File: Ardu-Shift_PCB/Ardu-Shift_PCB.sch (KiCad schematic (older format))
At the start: 18 parts, among them U1 OLED(SPI), U2 Arduino_Pro_Micro

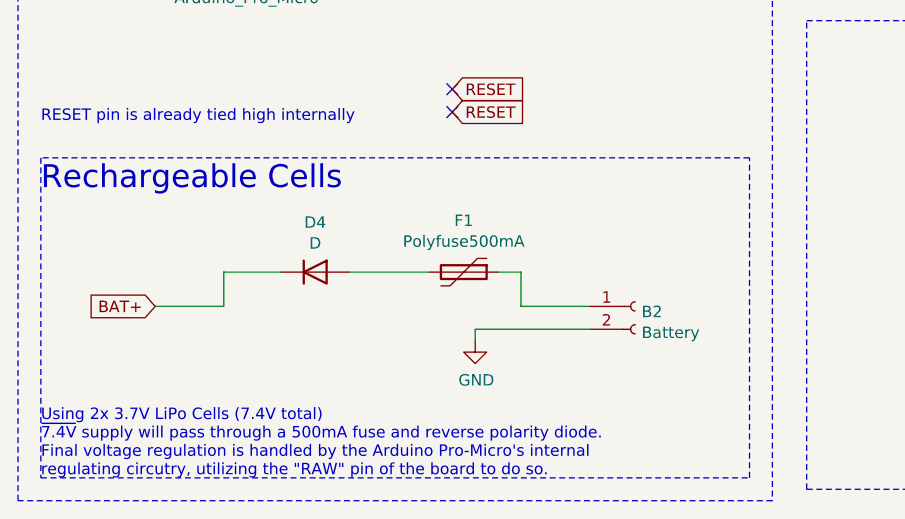
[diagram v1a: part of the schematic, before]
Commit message: added a power switch to ground for on/off functionality, added footprint for smaller speaker and updated all files.PDFs
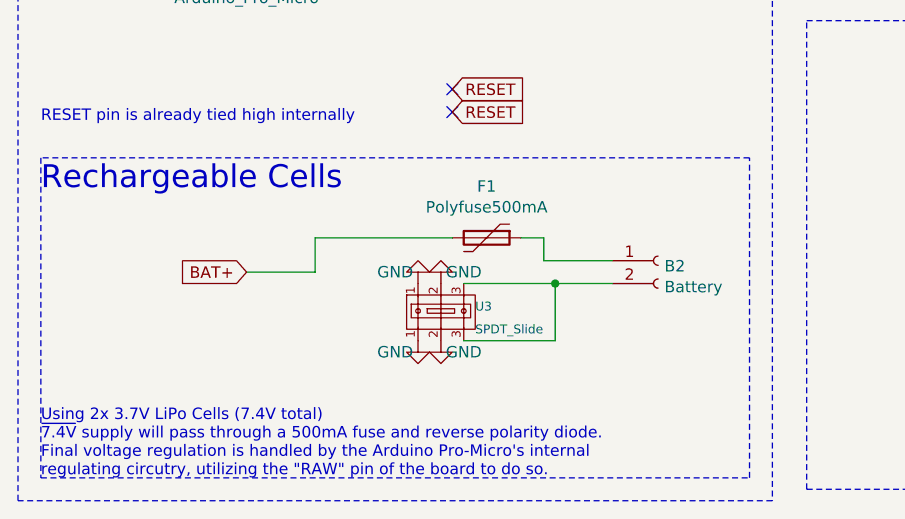
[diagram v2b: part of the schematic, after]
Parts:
- removed D4: D, Diode_THT:D_A-405_P10.16mm_Horizontal, symbol Device:D
- added U3: SPDT_Slide, Button_Switch_THT:SPDT_Slide, symbol Connector_Generic:SPDT_Slide
- LS1: footprint Resistor_THT:R_Axial_DIN0411_L9.9mm_D3.6mm_P15.24mm_Horizontal -> Buzzer_Beeper:Buzzer_12x9.5RM7.6
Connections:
- net BAT+: now also F1.2
- net GND: now also U3.1, U3.2; no longer B2.2 (Pin_2)
- new net: B2.2 (Pin_2), U3.3
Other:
- moved on the sheet: B2, F1
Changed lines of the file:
@@
 F 0 "LS1" V 3209 720 50  0000 R CNN
 F 1 "Speaker" V 3118 720 50  0000 R CNN
-F 2 "Resistor_THT:R_Axial_DIN0411_L9.9mm_D3.6mm_P15.24mm_Horizontal" H 3200 800 50  0001 C CNN
+F 2 "Buzzer_Beeper:Buzzer_12x9.5RM7.6" H 3200 800 50  0001 C CNN
 F 3 "~" H 3190 950 50  0001 C CNN
 	1    3200 1000
@@
 Text Notes 4200 800  0    100  ~ 0
 User Inputs\n
-Text GLabel 1250 6750 0    50   Input ~ 0
+Text GLabel 1650 6600 0    50   Input ~ 0
 BAT+
 Wire Notes Line
@@
 L Connector:Conn_01x02_Female B2
 U 1 1 603C890C
-P 3350 6750
-F 0 "B2" H 3378 6726 50  0000 L CNN
-F 1 "Battery" H 3378 6635 50  0000 L CNN
-F 2 "Connector_PinHeader_2.54mm:PinHeader_1x02_P2.54mm_Vertical" H 3350 6750 50  0001 C CNN
-F 3 "~" H 3350 6750 50  0001 C CNN
-	1    3350 6750
+P 3450 6550
+F 0 "B2" H 3478 6526 50  0000 L CNN
+F 1 "Battery" H 3478 6435 50  0000 L CNN
+F 2 "Connector_PinHeader_2.54mm:PinHeader_1x02_P2.54mm_Vertical" H 3450 6550 50  0001 C CNN
+F 3 "~" H 3450 6550 50  0001 C CNN
+	1    3450 6550
 	1    0    0    -1
 $EndComp
@@
 Wire Notes Line
 	3950 3650 3950 7600
-Text Notes 750  7500 0    50   ~ 0
-Using 2x 3.7V LiPo Cells (7.4V total)\n~7.4V supply will pass through a 500mA fuse and reverse polarity diode.\nFinal voltage regulation is handled by the Arduino Pro-Micro's internal \nregulating circutry, utilizing the "RAW" pin of the board to do so.
 Text Notes 800  3200 0    50   ~ 0
 Will be using THT for LEDs, Resistors, and Speaker \nTODO** determine resistor values for the LEDs michael has on hand\n
@@
 L Device:Polyfuse F1
 U 1 1 6044FB48
-P 2600 6600
-F 0 "F1" V 2375 6600 50  0000 C CNN
-F 1 "Polyfuse500mA" V 2466 6600 50  0000 C CNN
-F 2 "Resistor_THT:R_Axial_DIN0207_L6.3mm_D2.5mm_P7.62mm_Horizontal" H 2650 6400 50  0001 L CNN
-F 3 "~" H 2600 6600 50  0001 C CNN
-	1    2600 6600
-	0    1    1    0
-$EndComp
-Wire Wire Line
-	2750 6600 2850 6600
-Wire Wire Line
-	2850 6600 2850 6750
-Wire Wire Line
-	2850 6750 3150 6750
-$Comp
-L Device:D D4
-U 1 1 604552AC
-P 1950 6600
-F 0 "D4" H 1950 6817 50  0000 C CNN
-F 1 "D" H 1950 6726 50  0000 C CNN
-F 2 "Diode_THT:D_A-405_P10.16mm_Horizontal" H 1950 6600 50  0001 C CNN
-F 3 "~" H 1950 6600 50  0001 C CNN
-	1    1950 6600
-	1    0    0    -1
-$EndComp
-Wire Wire Line
-	1800 6600 1550 6600
-Wire Wire Line
-	1550 6600 1550 6750
-Wire Wire Line
-	1250 6750 1550 6750
-Wire Wire Line
-	2100 6600 2450 6600
+P 2700 6450
+F 0 "F1" V 2475 6450 50  0000 C CNN
+F 1 "Polyfuse500mA" V 2566 6450 50  0000 C CNN
+F 2 "Resistor_THT:R_Axial_DIN0207_L6.3mm_D2.5mm_P7.62mm_Horizontal" H 2750 6250 50  0001 L CNN
+F 3 "~" H 2700 6450 50  0001 C CNN
+	1    2700 6450
+	0    1    1    0
+$EndComp
+Wire Wire Line
+	2850 6450 2950 6450
+Wire Wire Line
+	2950 6450 2950 6550
+Wire Wire Line
+	2950 6550 3250 6550
+Wire Wire Line
+	1950 6450 1950 6600
+Wire Wire Line
+	1650 6600 1950 6600
 NoConn ~ 2550 5900
 NoConn ~ 1950 4400
-$Comp
-L power:GND #PWR0116
-U 1 1 6048AF00
-P 2650 6900
-F 0 "#PWR0116" H 2650 6650 50  0001 C CNN
-F 1 "GND" H 2655 6727 50  0000 C CNN
-F 2 "" H 2650 6900 50  0001 C CNN
-F 3 "" H 2650 6900 50  0001 C CNN
-	1    2650 6900
-	1    0    0    -1
-$EndComp
-Wire Wire Line
-	2650 6900 2650 6850
-Wire Wire Line
-	2650 6850 3150 6850
 Text GLabel 6450 1550 2    50   Input ~ 0
 A_Button
@@
 	6000 1750 6000 1650
 Connection ~ 6000 1650
+Wire Wire Line
+	1950 6450 2550 6450
+$Comp
+L Connector_Generic:SPDT_Slide U3
+U 1 1 604DA9EA
+P 2600 6650
+F 0 "U3" H 2650 6550 39  0000 L CNN
+F 1 "SPDT_Slide" H 2650 6450 39  0000 L CNN
+F 2 "Button_Switch_THT:SPDT_Slide" H 2600 6650 100 0001 C CNN
+F 3 "" H 2600 6650 100 0001 C CNN
+	1    2600 6650
+	1    0    0    -1
+$EndComp
+$Comp
+L power:GND #PWR0116
+U 1 1 604DE858
+P 2400 6900
+F 0 "#PWR0116" H 2400 6650 50  0001 C CNN
+F 1 "GND" H 2300 6850 50  0000 C CNN
+F 2 "" H 2400 6900 50  0001 C CNN
+F 3 "" H 2400 6900 50  0001 C CNN
+	1    2400 6900
+	1    0    0    -1
+$EndComp
+$Comp
+L power:GND #PWR0118
+U 1 1 604DF215
+P 2400 6650
+F 0 "#PWR0118" H 2400 6400 50  0001 C CNN
+F 1 "GND" H 2500 6600 50  0000 C CNN
+F 2 "" H 2400 6650 50  0001 C CNN
+F 3 "" H 2400 6650 50  0001 C CNN
+	1    2400 6650
+	-1   0    0    1
+$EndComp
+$Comp
+L power:GND #PWR0119
+U 1 1 604E087B
+P 2500 6650
+F 0 "#PWR0119" H 2500 6400 50  0001 C CNN
+F 1 "GND" H 2400 6600 50  0000 C CNN
+F 2 "" H 2500 6650 50  0001 C CNN
+F 3 "" H 2500 6650 50  0001 C CNN
+	1    2500 6650
+	-1   0    0    1
+$EndComp
+Wire Wire Line
+	2600 6650 3000 6650
+$Comp
+L power:GND #PWR0120
+U 1 1 604E65EA
+P 2500 6900
+F 0 "#PWR0120" H 2500 6650 50  0001 C CNN
+F 1 "GND" H 2600 6850 50  0000 C CNN
+F 2 "" H 2500 6900 50  0001 C CNN
+F 3 "" H 2500 6900 50  0001 C CNN
+	1    2500 6900
+	1    0    0    -1
+$EndComp
+Text Notes 750  7500 0    50   ~ 0
+Using 2x 3.7V LiPo Cells (7.4V total)\n~7.4V supply will pass through a 500mA fuse and reverse polarity diode.\nFinal voltage regulation is handled by the Arduino Pro-Micro's internal \nregulating circutry, utilizing the "RAW" pin of the board to do so.
+Wire Wire Line
+	2600 6900 3000 6900
+Wire Wire Line
+	3000 6900 3000 6650
+Connection ~ 3000 6650
+Wire Wire Line
+	3000 6650 3250 6650
 $EndSCHEMATC

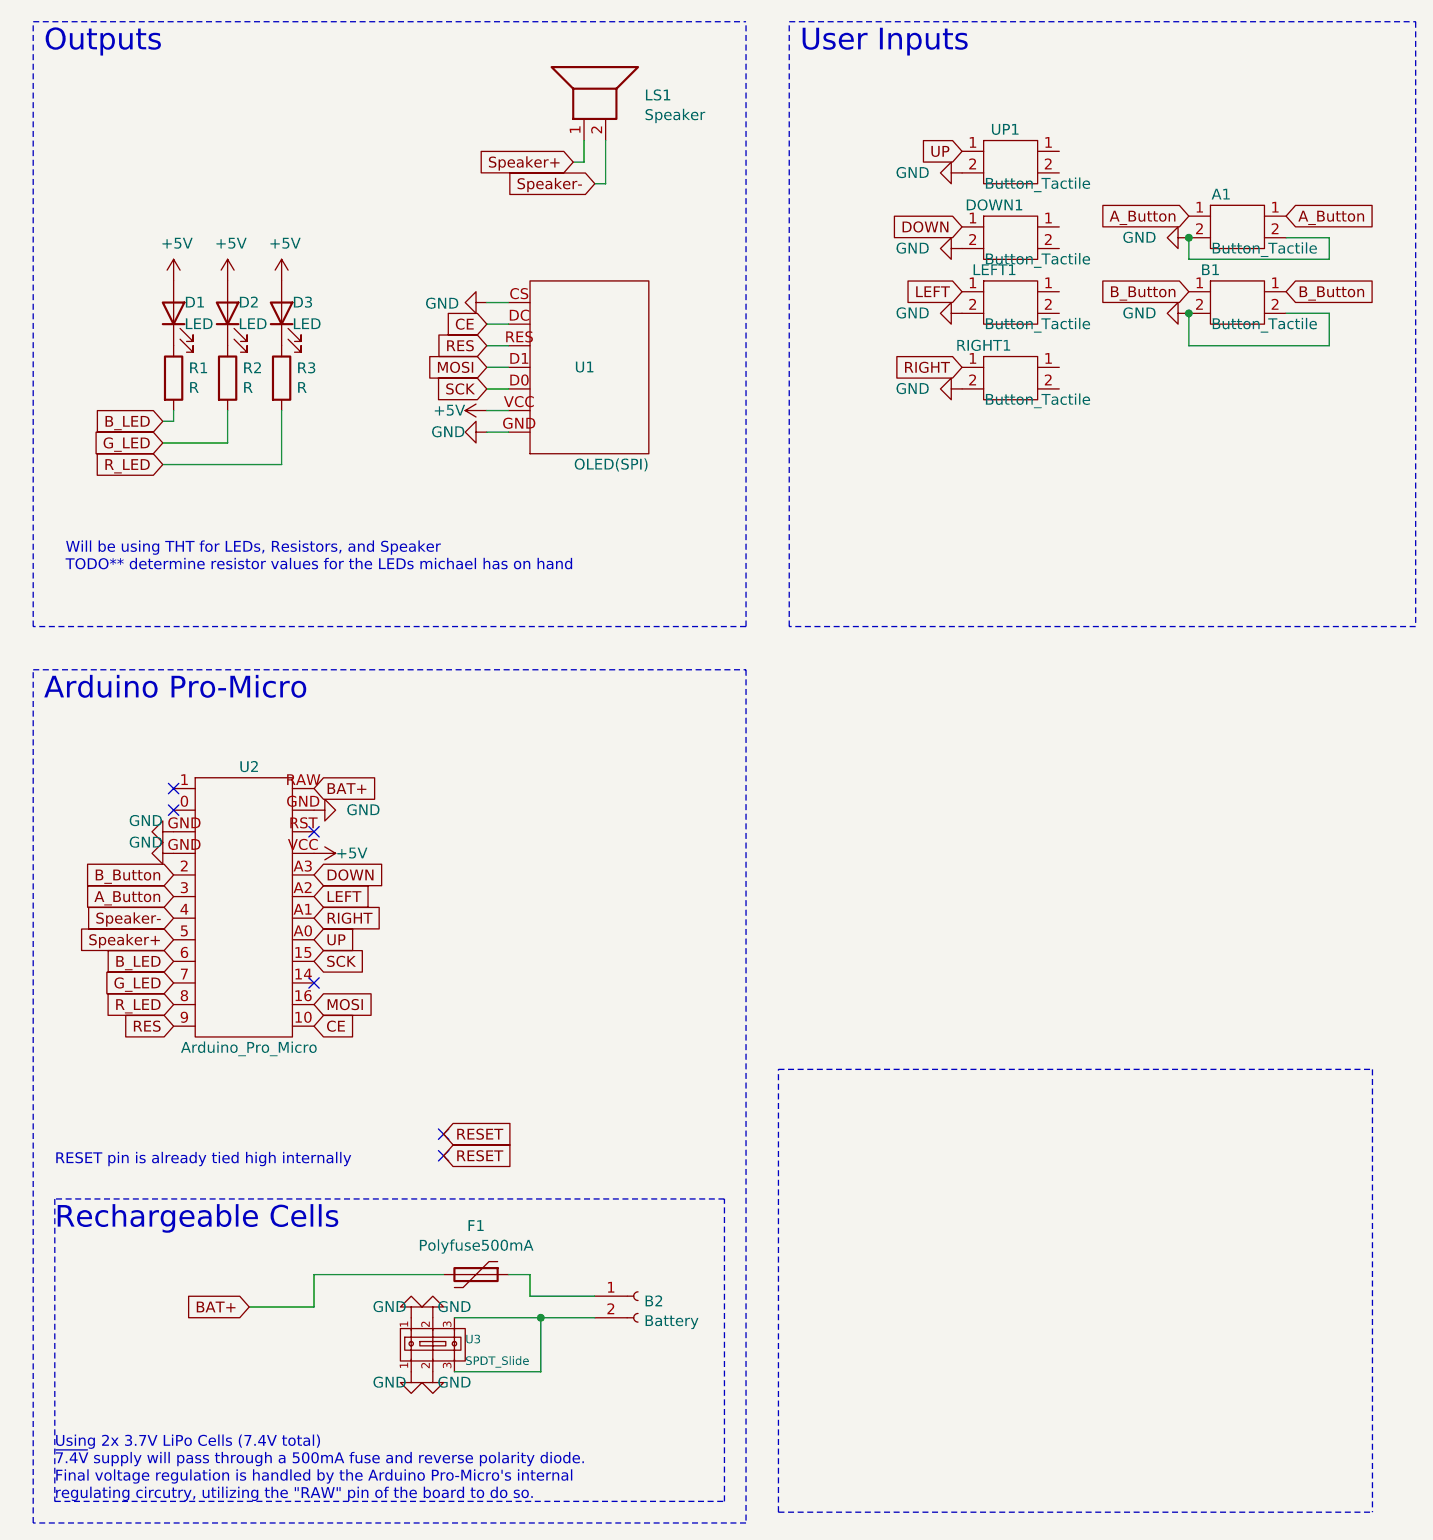
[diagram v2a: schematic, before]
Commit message: swapped pins on schematic/PCB to work with arduboy library
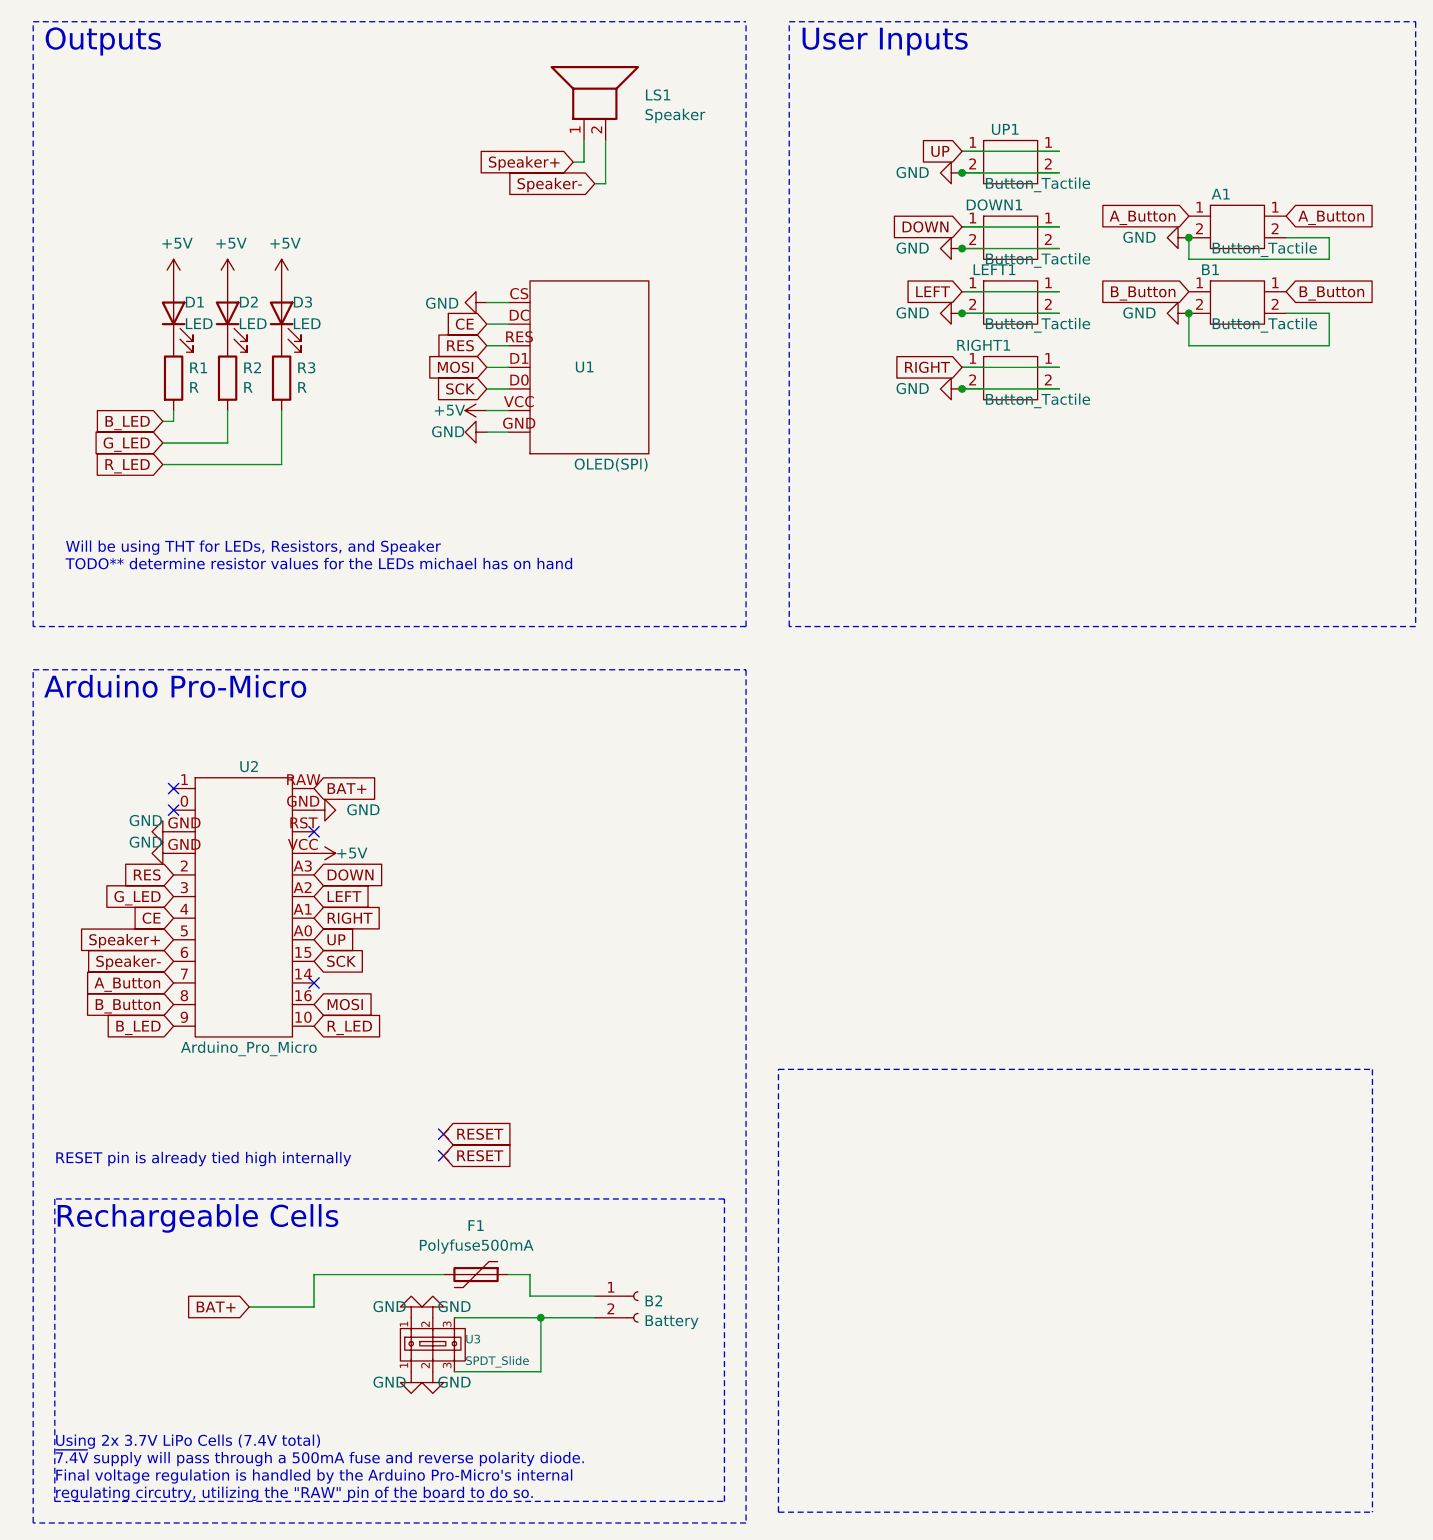
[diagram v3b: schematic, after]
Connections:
- net A_Button: now also U2.7; no longer U2.3
- net B_Button: now also U2.8; no longer U2.2
- net B_LED: now also U2.9; no longer U2.6
- net CE: now also U2.4; no longer U2.10
- net G_LED: now also U2.3; no longer U2.7
- net RES: now also U2.2; no longer U2.9
- net R_LED: now also U2.10; no longer U2.8
- net Speaker-: now also U2.6; no longer U2.4
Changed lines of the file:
@@
 Wire Wire Line
 	1250 2700 1800 2700
-Text GLabel 1300 5200 0    50   Input ~ 0
+Text GLabel 1950 5300 2    50   Input ~ 0
 R_LED
-Text GLabel 1300 5100 0    50   Input ~ 0
+Text GLabel 1300 4700 0    50   Input ~ 0
 G_LED
 $Comp
@@
 Text GLabel 2750 2050 0    50   Input ~ 0
 CE
-Text GLabel 1950 5300 2    50   Input ~ 0
+Text GLabel 1300 4800 0    50   Input ~ 0
 CE
 $Comp
@@
 Text GLabel 2750 2150 0    50   Input ~ 0
 RES
-Text GLabel 1300 5300 0    50   Input ~ 0
+Text GLabel 1300 4600 0    50   Input ~ 0
 RES
 Text GLabel 2550 5900 2    50   Input ~ 0
 RESET
-Text GLabel 1300 5000 0    50   Input ~ 0
+Text GLabel 1300 5300 0    50   Input ~ 0
 B_LED
 Text GLabel 1950 4900 2    50   Input ~ 0
@@
 Text Notes 750  5950 0    50   ~ 0
 RESET pin is already tied high internally\n
-Text GLabel 1300 4600 0    50   Input ~ 0
+Text GLabel 1300 5200 0    50   Input ~ 0
 B_Button
-Text GLabel 1300 4700 0    50   Input ~ 0
+Text GLabel 1300 5100 0    50   Input ~ 0
 A_Button
 $Comp
@@
 	0    1    1    0
 $EndComp
-Text GLabel 1300 4800 0    50   Input ~ 0
+Text GLabel 1300 5000 0    50   Input ~ 0
 Speaker-
 Text GLabel 1300 4900 0    50   Input ~ 0
@@
 Wire Wire Line
 	3000 6650 3250 6650
+Wire Wire Line
+	4950 1900 5400 1900
+Wire Wire Line
+	4950 2250 5400 2250
+Wire Wire Line
+	5400 1250 4950 1250
+Wire Wire Line
+	4950 1600 5400 1600
+Wire Wire Line
+	5400 1350 4950 1350
+Connection ~ 4950 1350
+Wire Wire Line
+	4950 1700 5400 1700
+Connection ~ 4950 1700
+Wire Wire Line
+	4950 2000 5400 2000
+Connection ~ 4950 2000
+Wire Wire Line
+	4950 2350 5400 2350
+Connection ~ 4950 2350
 $EndSCHEMATC
